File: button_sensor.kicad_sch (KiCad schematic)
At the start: 46 parts, among them J21 Conn_01x10, J22 Conn_01x10, U2 74HC138, U26 LTV-817S, U27 LTV-817S, U34 LTV-817S, U35 LTV-817S, U36 LTV-817S, U37 LTV-817S, U38 LTV-817S, U39 LTV-817S

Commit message: new file:   decon_ctrl.pdf
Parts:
- removed J21, J22: Conn_01x10, Connector_Phoenix_MC:PhoenixContact_MC_1,5_10-G-3.81_1x10_P3.81mm_Horizontal, symbol Connector_Generic:Conn_01x10
- removed R79, R80, R81, R82, R83, R84, R85, R86: 10K, Resistor_SMD:R_0805_2012Metric, symbol Device:R
- added R55, R56, R57, R58, R59, R60, R61, R62: 1K, Resistor_SMD:R_0805_2012Metric, symbol Device:R
- added R90, R91, R92, R93, R94, R95, R96, R97: 10K, Resistor_SMD:R_0805_2012Metric, symbol Device:R
- added U40, U41, U42, U43, U44, U45, U46, U47: LTV-817S, Package_DIP:SMDIP-4_W9.53mm, symbol Isolator:LTV-817S
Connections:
- net 3.3V: now also R90.1, R91.1, R92.1, R93.1, R94.1, R95.1, R96.1, R97.1
- net 74138_Y0: no longer R89.1, U2.3 (A2)
- net 74138_Y1: no longer R88.1, U2.2 (A1)
- net 74138_Y2: no longer R87.1, U2.1 (A0)
- net GND_MCU: now also U40.3, U41.3, U42.3, U43.3, U44.3, U45.3, U46.3, U47.3
- net MCU_BTN_0: now also R92.2, U42.4
- net MCU_BTN_1: now also R93.2, U43.4
- net MCU_BTN_2: now also R94.2, U44.4
- net MCU_BTN_3: now also R95.2, U45.4
- net MCU_BTN_4: now also R96.2, U46.4
- net MCU_BTN_5: now also R97.2, U47.4
- net VBAT: now also R55.1, R56.1, R57.1, R58.1, R59.1, R60.1, R61.1, R62.1
- new net: R59.2, U44.1
- new net: R61.2, U46.1
- new net: R62.2, U47.1
- new net: R55.2, U40.1
- new net: R57.2, U42.1
- new net: R58.2, U43.1
- new net: R60.2, U45.1
- new net: R56.2, U41.1
- new net BUTTON_0: U42.2
- new net BUTTON_1: U43.2
- new net BUTTON_2: U44.2
- new net BUTTON_3: U45.2
- new net BUTTON_4: U46.2
- new net BUTTON_5: U47.2
- new net MCU_A0: R87.1, U2.1 (A0)
- new net MCU_A1: R88.1, U2.2 (A1)
- new net MCU_A2: R89.1, U2.3 (A2)
- new net MCU_SS_0: R90.2, U40.4
- new net MCU_SS_1: R91.2, U41.4
- new net SENSOR_0: U40.2
- new net SENSOR_1: U41.2

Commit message: modified:   DECON_Ctrl_Panel.kicad_pcb
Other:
- moved on the sheet: R43, R44, R47, R48, R49, R50, R51, R52, R53, R54, R55, R56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

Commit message: modified:   DECON_Ctrl_Panel.kicad_pcb
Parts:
- removed R62: 1K, Resistor_SMD:R_0805_2012Metric, symbol Device:R
- removed R97: 10K, Resistor_SMD:R_0805_2012Metric, symbol Device:R
- removed U47: LTV-817S, Package_DIP:SMDIP-4_W9.53mm, symbol Isolator:LTV-817S
- added R128, R129: 1K, Resistor_SMD:R_0805_2012Metric, symbol Device:R
- added U36: LTV-817S, Package_DIP:SMDIP-4_W9.53mm, symbol Isolator:LTV-817S
- renumbered R91 to R100, R56 to R101, R92 to R102, R57 to R103, R43 to R104, R52 to R105, R93 to R106, R47 to R107, R71 to R108, R58 to R109, R48 to R110, R72 to R111, R94 to R112, R59 to R113, R49 to R114, R73 to R115, R95 to R116, R60 to R117, R44 to R118, R54 to R119, R96 to R120, R50 to R121, R74 to R122, R61 to R123, R51 to R124, R75 to R125, R53 to R126, R76 to R127, R65 to R90, R66 to R91, R67 to R92, R68 to R93, R69 to R94, R70 to R95, R77 to R96, R78 to R97, R90 to R98, R55 to R99, U40 to U20, U2 to U21, U41 to U22, U42 to U23, U26 to U24, U34 to U25, U43 to U26, U35 to U27, U44 to U28, U36 to U29, U45 to U30, U27 to U31, U37 to U32, U46 to U33, U38 to U34, U39 to U35
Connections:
- net 3.3V: now also R128.1
- net GND_MCU: now also U36.2
- net VBAT: now also R129.2
- net BUTTON_4 renamed EXT_INPUT
- net LED_7 renamed EXT_OUTPUT
- net MCU_BTN_4 renamed MCU_EXTI
- new net: R128.2, U36.1
- new net: R129.1, U36.4
- new net LED_POWER: U36.3

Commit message: modified:   DECON_Ctrl_Panel.kicad_pcb
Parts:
- renumbered R91 to R100, R92 to R101, R93 to R102, R94 to R103, R95 to R104, R96 to R105, R105 to R106, R108 to R107, R111 to R108, R115 to R109, R119 to R110, R122 to R111, R125 to R112, R127 to R113, R129 to R114, R97 to R115, R99 to R116, R101 to R117, R103 to R118, R109 to R119, R113 to R120, R117 to R121, R123 to R122, R98 to R123, R100 to R124, R102 to R125, R106 to R126, R112 to R127, R116 to R128, R120 to R129, R104 to R90, R107 to R91, R110 to R92, R114 to R93, R118 to R94, R121 to R95, R124 to R96, R126 to R97, R128 to R98, R90 to R99, U21 to U20, U24 to U21, U25 to U22, U27 to U23, U29 to U24, U31 to U25, U32 to U26, U34 to U27, U35 to U28, U36 to U29, U20 to U30, U22 to U31, U23 to U32, U26 to U33, U28 to U34, U30 to U35, U33 to U36

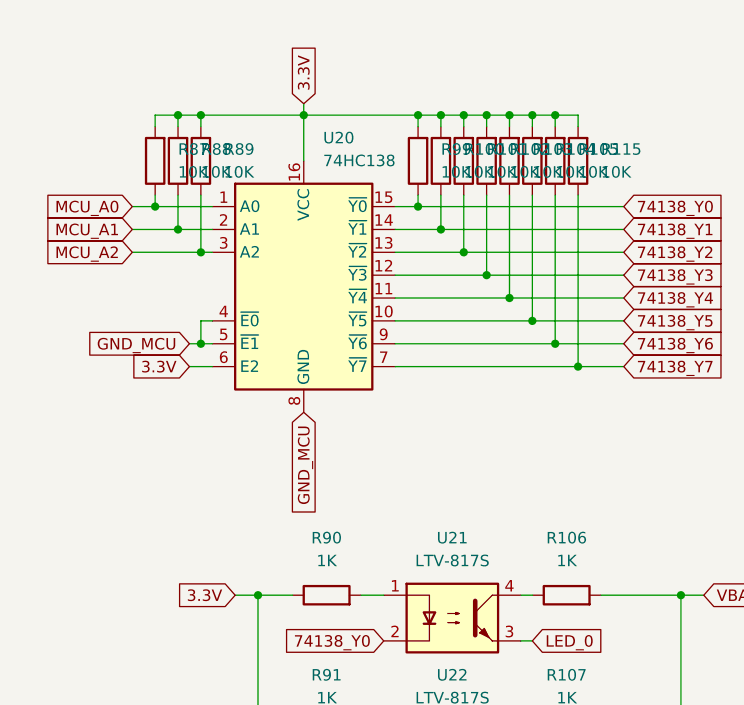
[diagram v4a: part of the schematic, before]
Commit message: modified:   DECON_Ctrl_Panel.kicad_pcb 	modified:   DECON_Ctrl_Panel.kicad_prl 	modified:   button_sensor.kicad_sch 	modified:   decon_mcu.kicad_sch
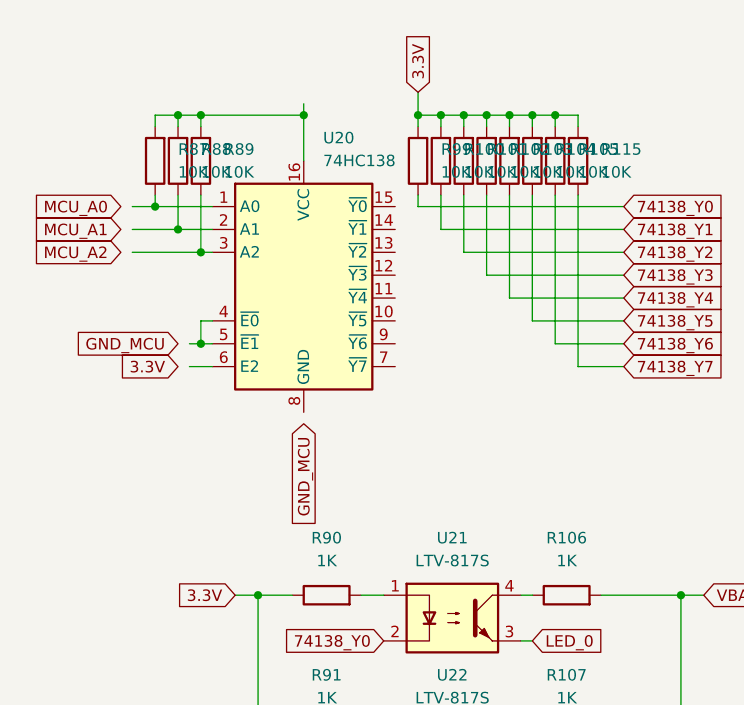
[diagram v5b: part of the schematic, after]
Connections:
- net 3.3V: no longer R87.2, R88.2, R89.2, U20.16 (VCC), U20.6 (E2)
- net 74138_Y0: no longer U20.15 (~{Y0})
- net 74138_Y1: no longer U20.14 (~{Y1})
- net 74138_Y2: no longer U20.13 (~{Y2})
- net 74138_Y3: no longer U20.12 (~{Y3})
- net 74138_Y4: no longer U20.11 (~{Y4})
- net 74138_Y5: no longer U20.10 (~{Y5})
- net 74138_Y6: no longer U20.9 (~{Y6})
- net 74138_Y7: no longer U20.7 (~{Y7})
- net GND_MCU: no longer U20.4 (~{E0}), U20.5 (~{E1}), U20.8 (GND)
- net MCU_A0: no longer R87.1, U20.1 (A0)
- net MCU_A1: no longer R88.1, U20.2 (A1)
- net MCU_A2: no longer R89.1, U20.3 (A2)
- new net: R88.1, U20.2 (A1)
- new net: R87.2, R88.2, R89.2, U20.16 (VCC)
- new net: R89.1, U20.3 (A2)
- new net: R87.1, U20.1 (A0)
- new net: U20.4 (~{E0}), U20.5 (~{E1})
